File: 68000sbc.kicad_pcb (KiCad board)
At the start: 2 copper layers, 127 x 90.8 mm, 49 parts, among them J1 USB_B, J2 5V FTDI SERIAL, J3 RTC (SparkFun BOB-10160), J4 CFCARD/IDE, J5 EXPANSION (F.Cu), J6 EXPANSION (B.Cu), SW1 RESET, SW2 BTN1, U1 74HC139, U2 74HC14, U3 TMP68HC000P-12, U4 AS6C4008-55PCN, U5 28C256, U6 AS6C4008-55PCN, U7 28C256, U8 TL16C550, X1 12MHz, X2 12MHz

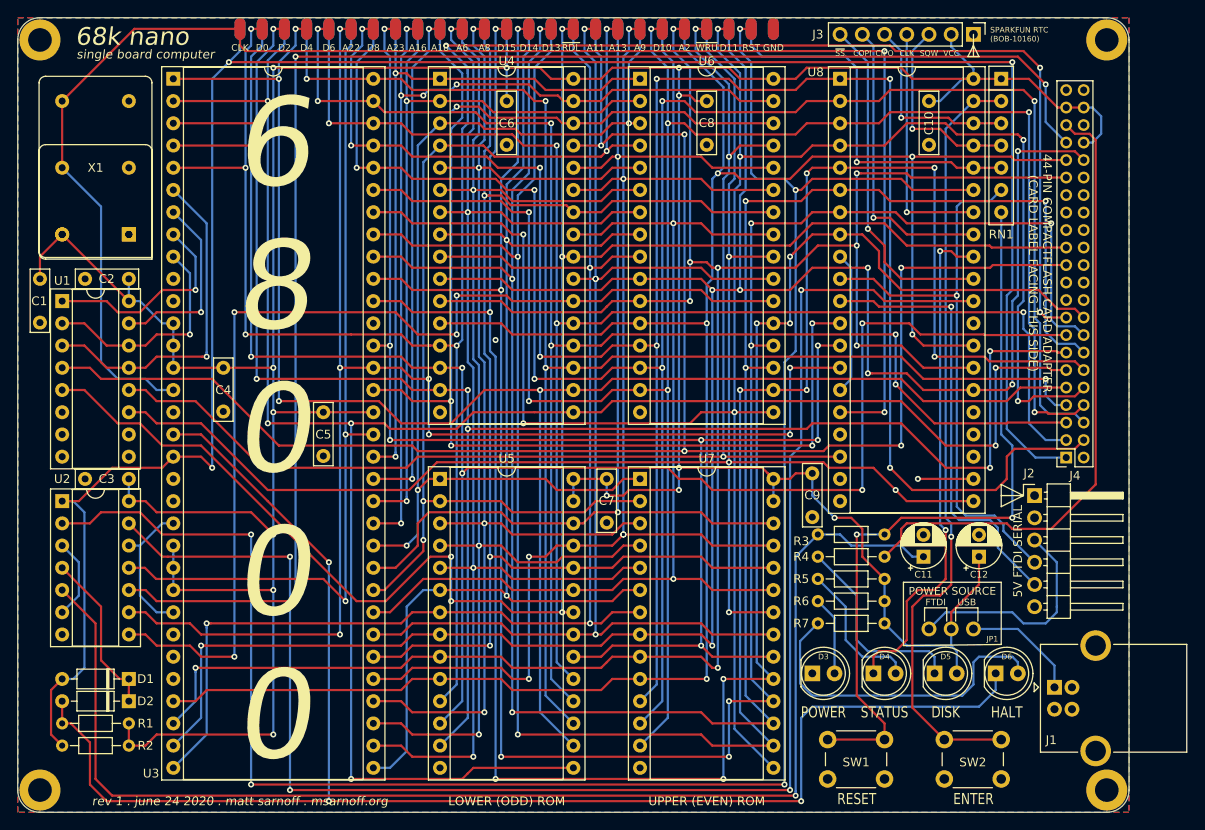
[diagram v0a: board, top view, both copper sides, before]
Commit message: Fix track width for JLC requirements
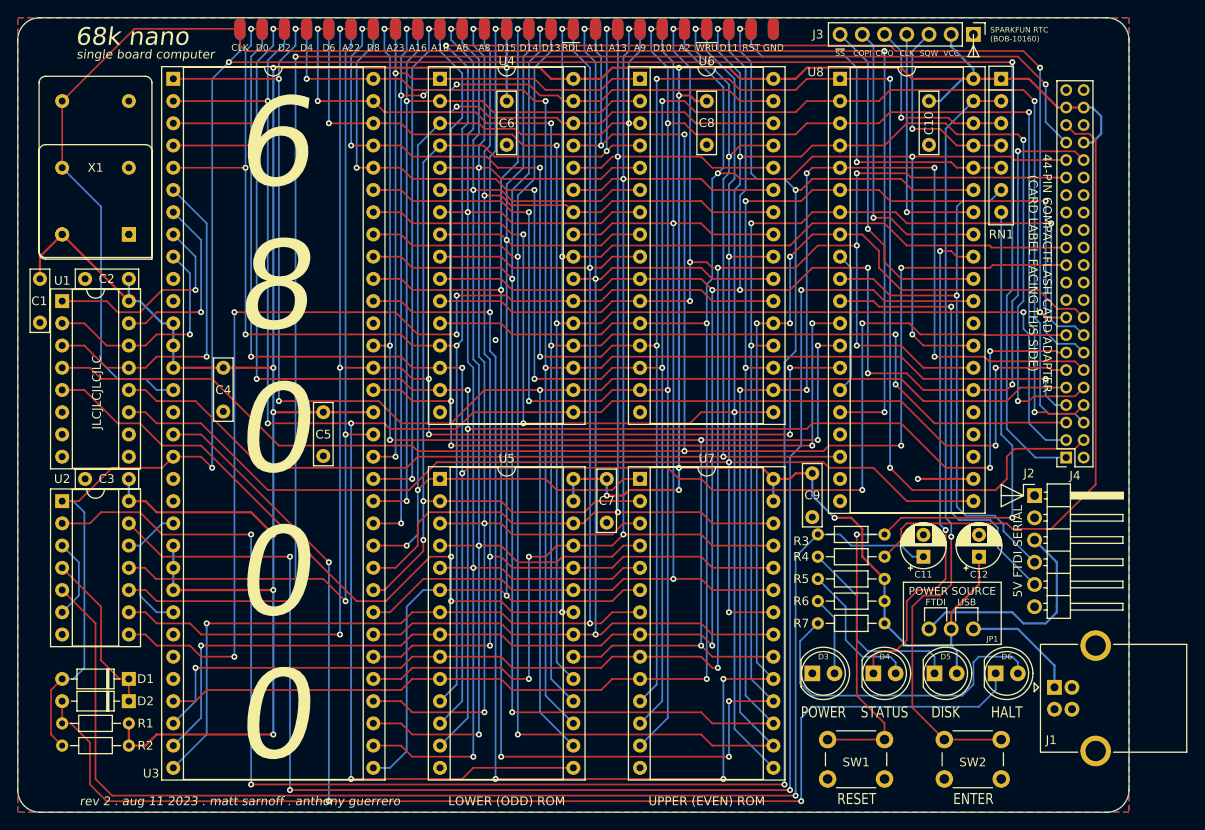
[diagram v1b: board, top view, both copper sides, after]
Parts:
- removed REF** (x4): MountingHole_2.7mm_M2.5_DIN965_Pad, MountingHole:MountingHole_2.7mm_M2.5_DIN965_Pad
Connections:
- net /R,~W renamed /R,~{W}
- net /~A20 renamed /~{A20}
- net /~A22 renamed /~{A22}
- net /~AS renamed /~{AS}
- net /~BTN1 renamed /~{BTN1}
- net /~CFLED renamed /~{CFLED}
- net /~HALT renamed /~{HALT}
- net /~IRQ renamed /~{IRQ}
- net /~LDS renamed /~{LDS}
- net /~RDL renamed /~{RDL}
- net /~RDU renamed /~{RDU}
- net /~RESET renamed /~{RESET}
- net /~RESETBTN renamed /~{RESETBTN}
- net /~RTC_SS renamed /~{RTC_SS}
- net /~UDS renamed /~{UDS}
- net /~WRL renamed /~{WRL}
- net /~WRU renamed /~{WRU}
- J1 pad 2: Net-(J1-Pad2) -> unconnected-(J1-D--Pad2)
- J1 pad 3: Net-(J1-Pad3) -> unconnected-(J1-D+-Pad3)
- J2 pad 2: Net-(J2-Pad2) -> unconnected-(J2-Pin_2-Pad2)
- J2 pad 6: Net-(J2-Pad6) -> unconnected-(J2-Pin_6-Pad6)
- J4 pad 20: Net-(J4-Pad20) -> unconnected-(J4-Pin_20-Pad20)
- J4 pad 21: Net-(J4-Pad21) -> unconnected-(J4-Pin_21-Pad21)
- J4 pad 27: Net-(J4-Pad27) -> unconnected-(J4-Pin_27-Pad27)
- J4 pad 28: Net-(J4-Pad28) -> unconnected-(J4-Pin_28-Pad28)
- J4 pad 29: Net-(J4-Pad29) -> unconnected-(J4-Pin_29-Pad29)
- J4 pad 32: Net-(J4-Pad32) -> unconnected-(J4-Pin_32-Pad32)
- J4 pad 34: Net-(J4-Pad34) -> unconnected-(J4-Pin_34-Pad34)
- J4 pad 44: Net-(J4-Pad44) -> unconnected-(J4-Pin_44-Pad44)
- U1 pad 10: Net-(U1-Pad10) -> unconnected-(U1B-O2-Pad10)
- U1 pad 6: Net-(U1-Pad6) -> unconnected-(U1A-O2-Pad6)
- U1 pad 7: Net-(U1-Pad7) -> unconnected-(U1A-O3-Pad7)
- U1 pad 9: Net-(U1-Pad9) -> unconnected-(U1B-O3-Pad9)
- U3 pad 11: Net-(U3-Pad11) -> unconnected-(U3-BG-Pad11)
- U3 pad 19: Net-(U3-Pad19) -> unconnected-(U3-VMA-Pad19)
- U3 pad 20: Net-(U3-Pad20) -> unconnected-(U3-E-Pad20)
- U3 pad 26: Net-(U3-Pad26) -> unconnected-(U3-FC2-Pad26)
- U3 pad 27: Net-(U3-Pad27) -> unconnected-(U3-FC1-Pad27)
- U3 pad 28: Net-(U3-Pad28) -> unconnected-(U3-FC0-Pad28)
- U8 pad 17: Net-(U8-Pad17) -> unconnected-(U8-XOUT-Pad17)
- U8 pad 23: Net-(U8-Pad23) -> unconnected-(U8-DDIS-Pad23)
- U8 pad 24: Net-(U8-Pad24) -> unconnected-(U8-~{TXRDY}-Pad24)
- U8 pad 29: Net-(U8-Pad29) -> unconnected-(U8-~{RXRDY}-Pad29)
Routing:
- net /A18: track 102.0 -> 101.3 mm
- net /A15: track 116.5 -> 115.9 mm
- net VCC: track 443.3 -> 442.7 mm
- net /~{RDU}: vias 4 -> 3
- net /A9: vias 6 -> 5
- net /A11: vias 4 -> 3
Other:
- net class Default removed
- net class Thicc removed
- rule pad_to_mask_clearance: 0.051 -> 0
- board text added: "JLCJLCJLCJLC"
- board text added: "R/~{W}"
- board text added: "rev 2 . aug 11 2023 . matt sarnoff . anthony guerrero"
- board text added: "~{AS}"
- board text added: "~{BERR}"
- board text added: "~{BGACK}"
- board text added: "~{BG}"
- board text added: "~{BR}"
- board text added: "~{DTACK}"
- board text added: "~{DTACK} GROUNDED!!"
- board text added: "~{HALT}"
- board text added: "~{IPL0}"
- board text added: "~{IPL1}"
- board text added: "~{IPL2}"
- board text added: "~{LDS}"
- board text added: "~{RDL}"
- board text added: "~{RDU}"
- board text added: "~{RESET}"
- board text added: "~{RST}"
- board text added: "~{SS}"
- board text added: "~{UDS}"
- board text added: "~{VMA}"
- board text added: "~{VPA}"
- board text added: "~{WRL}"
- board text added: "~{WRU}"
- board text removed: "R/~W"
- board text removed: "rev 1 . june 24 2020 . matt sarnoff . msarnoff.org"
- board text removed: "~AS"
- board text removed: "~BERR"
- board text removed: "~BG"
- board text removed: "~BGACK"
- board text removed: "~BR"
- board text removed: "~DTACK"
- board text removed: "~DTACK~ GROUNDED!!"
- board text removed: "~HALT"
- board text removed: "~IPL0"
- board text removed: "~IPL1"
- board text removed: "~IPL2"
- board text removed: "~LDS"
- board text removed: "~RDL"
- board text removed: "~RDU"
- board text removed: "~RESET"
- board text removed: "~RST"
- board text removed: "~SS"
- board text removed: "~UDS"
- board text removed: "~VMA"
- board text removed: "~VPA"
- board text removed: "~WRL"
- board text removed: "~WRU"
